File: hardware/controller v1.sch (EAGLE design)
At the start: 35 parts, among them CON1 1X08-CONN3.5MM, CON2 1X08-CONN3.5MM, CON3 1X08-CONN3.5MM, CON4 1X08-CONN3.5MM, IC1 MC33880PEG, IC2 L293DD, IC3 MC33880PEG

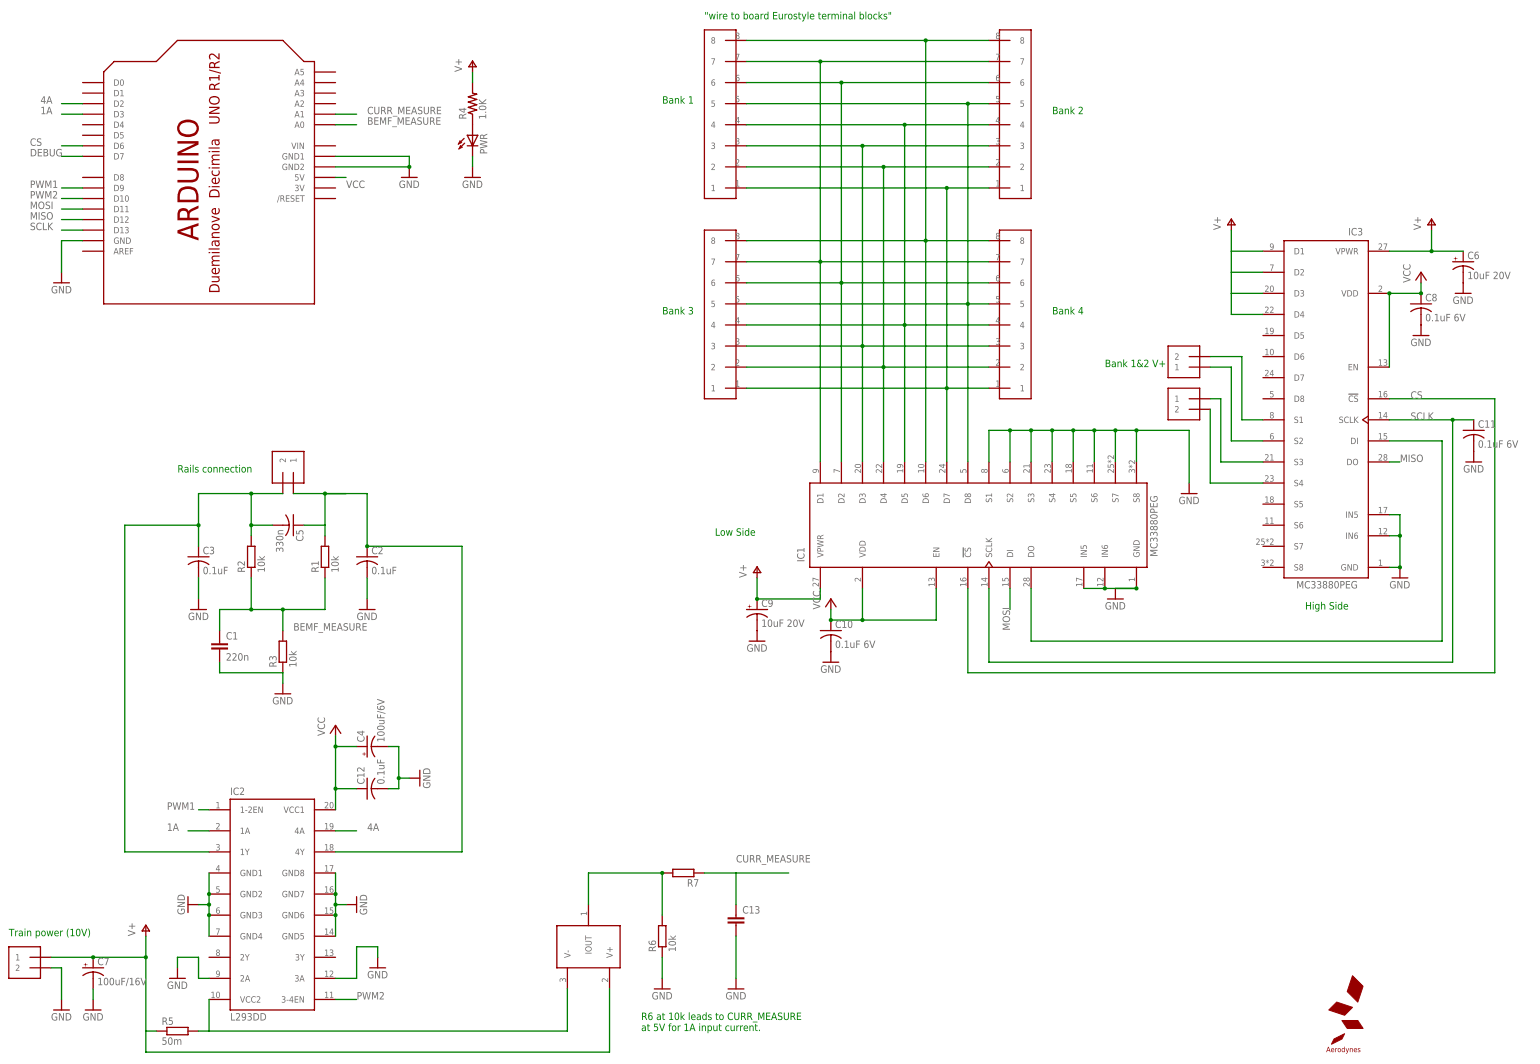
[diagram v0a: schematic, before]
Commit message: Update on board layout for Arduino shield.
Better layout, added component names.
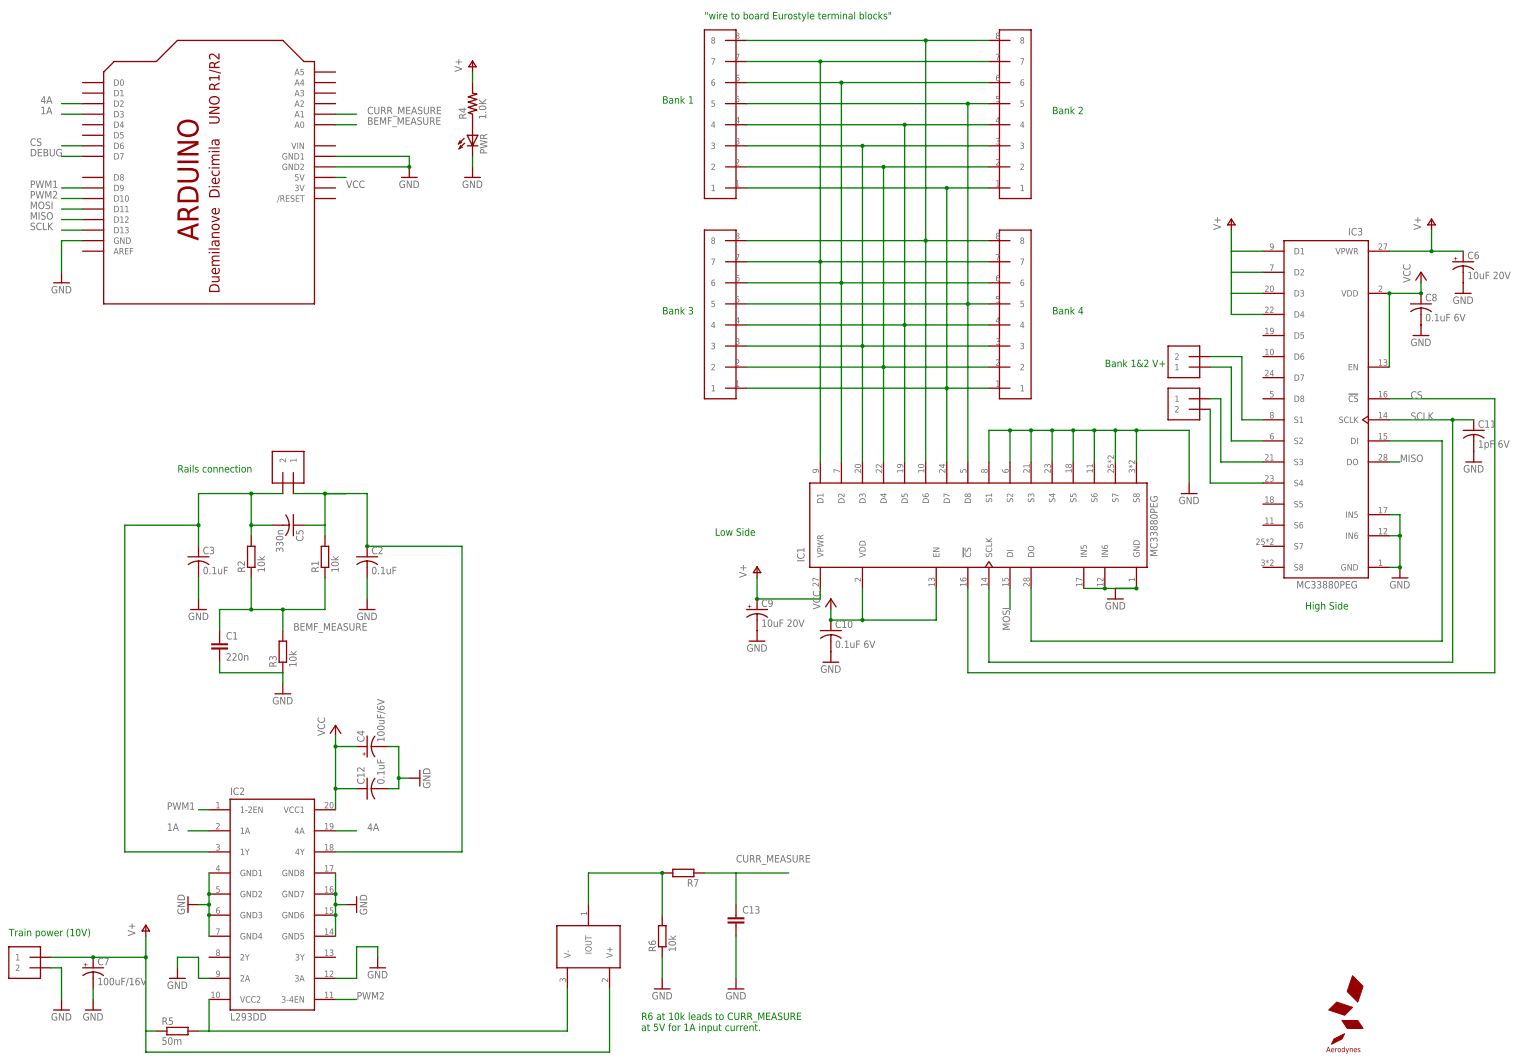
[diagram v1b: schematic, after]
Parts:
- C11: value 0.1uF 6V -> 1pF 6V
- IC2: device l293dd:L293DD" -> aerodynes:L293DD
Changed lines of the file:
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@@
 </classes>
 <parts>
-<part name="IC2" library="l293dd" deviceset="L293DD" device="&quot;" value="L293DD"/>
+<part name="IC2" library="aerodynes" deviceset="L293D" device="D" value="L293DD"/>
 <part name="SL1" library="adafruit" deviceset="1X2" device="-3.5MM"/>
 <part name="GND1" library="supply1" deviceset="GND" device=""/>
@@
 <part name="GND13" library="supply1" deviceset="GND" device=""/>
 <part name="GND14" library="supply1" deviceset="GND" device=""/>
-<part name="C11" library="rcl-ez" deviceset="C-US" device="025-025X050" value="0.1uF 6V"/>
+<part name="C11" library="rcl-ez" deviceset="C-US" device="025-025X050" value="1pF 6V"/>
 <part name="GND15" library="supply1" deviceset="GND" device=""/>
 <part name="BANK12" library="adafruit" deviceset="1X2" device="-3.5MM"/>
@@
 </plain>
 <instances>
-<instance part="IC2" gate="G$1" x="40.64" y="-12.7"/>
+<instance part="IC2" gate="G$1" x="40.64" y="-7.62"/>
 <instance part="SL1" gate="G$1" x="43.18" y="93.98" rot="MR90"/>
 <instance part="GND1" gate="1" x="20.32" y="-10.16" rot="R270"/>

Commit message: Diagnostics screen works now!
Complete board diagnostics, including port open circuit detection.
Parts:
- C11: device rcl-ez:C-US025-025X050 -> rcl-ez:C-USC0805K
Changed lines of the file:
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@@
 <grid distance="0.1" unitdist="inch" unit="inch" style="lines" multiple="1" display="no" altdistance="0.01" altunitdist="inch" altunit="inch"/>
 <layers>
-<layer number="1" name="Top" color="4" fill="1" visible="no" active="no"/>
-<layer number="2" name="Route2" color="1" fill="3" visible="no" active="no"/>
-<layer number="3" name="Route3" color="4" fill="3" visible="no" active="no"/>
-<layer number="4" name="Route4" color="1" fill="4" visible="no" active="no"/>
-<layer number="5" name="Route5" color="4" fill="4" visible="no" active="no"/>
-<layer number="6" name="Route6" color="1" fill="8" visible="no" active="no"/>
-<layer number="7" name="Route7" color="4" fill="8" visible="no" active="no"/>
-<layer number="8" name="Route8" color="1" fill="2" visible="no" active="no"/>
-<layer number="9" name="Route9" color="4" fill="2" visible="no" active="no"/>
-<layer number="10" name="Route10" color="1" fill="7" visible="no" active="no"/>
-<layer number="11" name="Route11" color="4" fill="7" visible="no" active="no"/>
-<layer number="12" name="Route12" color="1" fill="5" visible="no" active="no"/>
-<layer number="13" name="Route13" color="4" fill="5" visible="no" active="no"/>
-<layer number="14" name="Route14" color="1" fill="6" visible="no" active="no"/>
-<layer number="15" name="Route15" color="4" fill="6" visible="no" active="no"/>
-<layer number="16" name="Bottom" color="1" fill="1" visible="no" active="no"/>
-<layer number="17" name="Pads" color="2" fill="1" visible="no" active="no"/>
-<layer number="18" name="Vias" color="2" fill="1" visible="no" active="no"/>
-<layer number="19" name="Unrouted" color="6" fill="1" visible="no" active="no"/>
-<layer number="20" name="Dimension" color="15" fill="1" visible="no" active="no"/>
-<layer number="21" name="tPlace" color="7" fill="1" visible="no" active="no"/>
-<layer number="22" name="bPlace" color="7" fill="1" visible="no" active="no"/>
-<layer number="23" name="tOrigins" color="15" fill="1" visible="no" active="no"/>
-<layer number="24" name="bOrigins" color="15" fill="1" visible="no" active="no"/>
-<layer number="25" name="tNames" color="7" fill="1" visible="no" active="no"/>
-<layer number="26" name="bNames" color="7" fill="1" visible="no" active="no"/>
-<layer number="27" name="tValues" color="7" fill="1" visible="no" active="no"/>
-<layer number="28" name="bValues" color="7" fill="1" visible="no" active="no"/>
+<layer number="1" name="Top" color="4" fill="1" visible="yes" active="no"/>
+<layer number="2" name="Route2" color="1" fill="3" visible="yes" active="no"/>
+<layer number="3" name="Route3" color="4" fill="3" visible="yes" active="no"/>
+<layer number="4" name="Route4" color="1" fill="4" visible="yes" active="no"/>
+<layer number="5" name="Route5" color="4" fill="4" visible="yes" active="no"/>
+<layer number="6" name="Route6" color="1" fill="8" visible="yes" active="no"/>
+<layer number="7" name="Route7" color="4" fill="8" visible="yes" active="no"/>
+<layer number="8" name="Route8" color="1" fill="2" visible="yes" active="no"/>
+<layer number="9" name="Route9" color="4" fill="2" visible="yes" active="no"/>
+<layer number="10" name="Route10" color="1" fill="7" visible="yes" active="no"/>
+<layer number="11" name="Route11" color="4" fill="7" visible="yes" active="no"/>
+<layer number="12" name="Route12" color="1" fill="5" visible="yes" active="no"/>
+<layer number="13" name="Route13" color="4" fill="5" visible="yes" active="no"/>
+<layer number="14" name="Route14" color="1" fill="6" visible="yes" active="no"/>
+<layer number="15" name="Route15" color="4" fill="6" visible="yes" active="no"/>
+<layer number="16" name="Bottom" color="1" fill="1" visible="yes" active="no"/>
+<layer number="17" name="Pads" color="2" fill="1" visible="yes" active="no"/>
+<layer number="18" name="Vias" color="2" fill="1" visible="yes" active="no"/>
+<layer number="19" name="Unrouted" color="6" fill="1" visible="yes" active="no"/>
+<layer number="20" name="Dimension" color="15" fill="1" visible="yes" active="no"/>
+<layer number="21" name="tPlace" color="7" fill="1" visible="yes" active="no"/>
+<layer number="22" name="bPlace" color="7" fill="1" visible="yes" active="no"/>
+<layer number="23" name="tOrigins" color="15" fill="1" visible="yes" active="no"/>
+<layer number="24" name="bOrigins" color="15" fill="1" visible="yes" active="no"/>
+<layer number="25" name="tNames" color="7" fill="1" visible="yes" active="no"/>
+<layer number="26" name="bNames" color="7" fill="1" visible="yes" active="no"/>
+<layer number="27" name="tValues" color="7" fill="1" visible="yes" active="no"/>
+<layer number="28" name="bValues" color="7" fill="1" visible="yes" active="no"/>
 <layer number="29" name="tStop" color="7" fill="3" visible="no" active="no"/>
 <layer number="30" name="bStop" color="7" fill="6" visible="no" active="no"/>
@@
 <layer number="35" name="tGlue" color="7" fill="4" visible="no" active="no"/>
 <layer number="36" name="bGlue" color="7" fill="5" visible="no" active="no"/>
-<layer number="37" name="tTest" color="7" fill="1" visible="no" active="no"/>
-<layer number="38" name="bTest" color="7" fill="1" visible="no" active="no"/>
+<layer number="37" name="tTest" color="7" fill="1" visible="yes" active="no"/>
+<layer number="38" name="bTest" color="7" fill="1" visible="yes" active="no"/>
 <layer number="39" name="tKeepout" color="4" fill="11" visible="no" active="no"/>
 <layer number="40" name="bKeepout" color="1" fill="11" visible="no" active="no"/>
@@
 <layer number="44" name="Drills" color="7" fill="1" visible="no" active="no"/>
 <layer number="45" name="Holes" color="7" fill="1" visible="no" active="no"/>
-<layer number="46" name="Milling" color="3" fill="1" visible="no" active="no"/>
-<layer number="47" name="Measures" color="7" fill="1" visible="no" active="no"/>
-<layer number="48" name="Document" color="7" fill="1" visible="no" active="no"/>
-<layer number="49" name="Reference" color="7" fill="1" visible="no" active="no"/>
-<layer number="50" name="dxf" color="7" fill="1" visible="no" active="no"/>
-<layer number="51" name="tDocu" color="7" fill="1" visible="no" active="no"/>
-<layer number="52" name="bDocu" color="7" fill="1" visible="no" active="no"/>
-<layer number="53" name="tGND_GNDA" color="7" fill="9" visible="no" active="no"/>
-<layer number="54" name="bGND_GNDA" color="1" fill="9" visible="no" active="no"/>
-<layer number="56" name="wert" color="7" fill="1" visible="no" active="no"/>
+<layer number="46" name="Milling" color="3" fill="1" visible="yes" active="no"/>
+<layer number="47" name="Measures" color="7" fill="1" visible="yes" active="no"/>
+<layer number="48" name="Document" color="7" fill="1" visible="yes" active="no"/>
+<layer number="49" name="Reference" color="7" fill="1" visible="yes" active="no"/>
+<layer number="50" name="dxf" color="7" fill="1" visible="yes" active="no"/>
+<layer number="51" name="tDocu" color="7" fill="1" visible="yes" active="no"/>
+<layer number="52" name="bDocu" color="7" fill="1" visible="yes" active="no"/>
+<layer number="53" name="tGND_GNDA" color="7" fill="9" visible="yes" active="no"/>
+<layer number="54" name="bGND_GNDA" color="1" fill="9" visible="yes" active="no"/>
+<layer number="56" name="wert" color="7" fill="1" visible="yes" active="no"/>
 <layer number="91" name="Nets" color="2" fill="1" visible="yes" active="yes"/>
 <layer number="92" name="Busses" color="1" fill="1" visible="yes" active="yes"/>
@@
 <part name="GND13" library="supply1" deviceset="GND" device=""/>
 <part name="GND14" library="supply1" deviceset="GND" device=""/>
-<part name="C11" library="rcl-ez" deviceset="C-US" device="025-025X050" value="1pF 6V"/>
+<part name="C11" library="rcl-ez" deviceset="C-US" device="C0805K" value="1pF 6V"/>
 <part name="GND15" library="supply1" deviceset="GND" device=""/>
 <part name="BANK12" library="adafruit" deviceset="1X2" device="-3.5MM"/>
